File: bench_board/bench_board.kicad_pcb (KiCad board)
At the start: 4 copper layers, 80 x 60 mm, 42 parts, among them J1 BATT_2S, J2 BOOT0_JUMPER, J3 USB-C, J4 CRSF_UART, J5 DSHOT_M1-M4, J6 SWD, U1 STM32F405RGT6, U2 TPS563201, U3 AMS1117-3.3, U4 MPU-6000, U5 USBLC6-2SC6, Y1 8MHz

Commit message: Rework power tree to single-stage buck (3.3V direct); add battery-sense divider
Deletes the AMS1117 5V->3.3V LDO stage and its caps -- the 2-stage
buck-then-LDO topology forced the buck to hold 5V from a 2S pack whose
6.0V floor leaves only 1V of headroom (~83% duty cycle, at/past most buck
ICs' practical limit). TPS563201 now regulates directly to 3.3V (feedback
divider R1/R2 retargeted: 33.2k/10.0k, Vref=0.768V -> ~3.30V), which is
what every load on this board (STM32F405, MPU-6000, DShot signal levels)
actually wants. Duty cycle at 6.0V floor is now ~55%; at 8.4V ceiling
~39% -- comfortable across the whole battery range, both ends far from the
TPS563201's ~90% max-duty limit.

Inductor re-sized for the new operating point: L1 2.2uH -> 10uH, sized for
~23% ripple current at a 1.5A load estimate (worst-case ripple is at
Vin=8.4V, the max input, not the 6.0V floor). C2 (22uF output cap,
unchanged) gives ~7mV ripple at that current, comfortable margin. Thermal
margin is now single-stage only (~0.5W in the buck at 1.5A/90% eff, ~33C
rise in a SOT-23-6 package) instead of also carrying the LDO's dropout
heat, which was the dominant loss term in the old topology.

Also fixed a real latent bug found while touching this circuit: C3, the
TPS563201's SW-to-BOOST bootstrap cap, was 2.2nF -- roughly two orders of
magnitude under the ~100nF a D-CAP2/D-CAP3 synchronous buck needs to hold
the high-side gate charge, especially at the now-much-lower duty cycles.
Corrected to 100nF.

CRSF_UART's receiver-power pin (J4/1) now carries 3V3 instead of the
deleted 5V rail. Per the Build Plan: the many 5V-only ELRS nano receivers
this affects get resolved by picking a 3.3V-capable receiver in Stage 2
part selection, not by adding a rail back.

Battery-sense divider added (genuine prior omission -- no low-voltage
cutoff existed anywhere): R9 (20.0k, VBAT_2S side) / R10 (10.0k, GND
side), 1% resistors, into PA0 (ADC123_IN0, previously unused) with a
100nF filter cap (C22). Divide-by-3.0 r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
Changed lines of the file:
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@@
 		(end 3 0)
 		(stroke
-			(width 0)
+			(width 0.1)
 			(type default)
 		)
@@
 		(end 0 3)
 		(stroke
-			(width 0)
+			(width 0.1)
 			(type default)
 		)
@@
 		(end 77 0)
 		(stroke
-			(width 0)
+			(width 0.1)
 			(type default)
 		)
@@
 		(end 0 57)
 		(stroke
-			(width 0)
+			(width 0.1)
 			(type default)
 		)
@@
 		(end 80 3)
 		(stroke
-			(width 0)
+			(width 0.1)
 			(type default)
 		)
@@
 		(end 3 60)
 		(stroke
-			(width 0)
+			(width 0.1)
 			(type default)
 		)
@@
 		(end 80 57)
 		(stroke
-			(width 0)
+			(width 0.1)
 			(type default)
 		)
@@
 		(end 77 60)
 		(stroke
-			(width 0)
+			(width 0.1)
 			(type default)
 		)

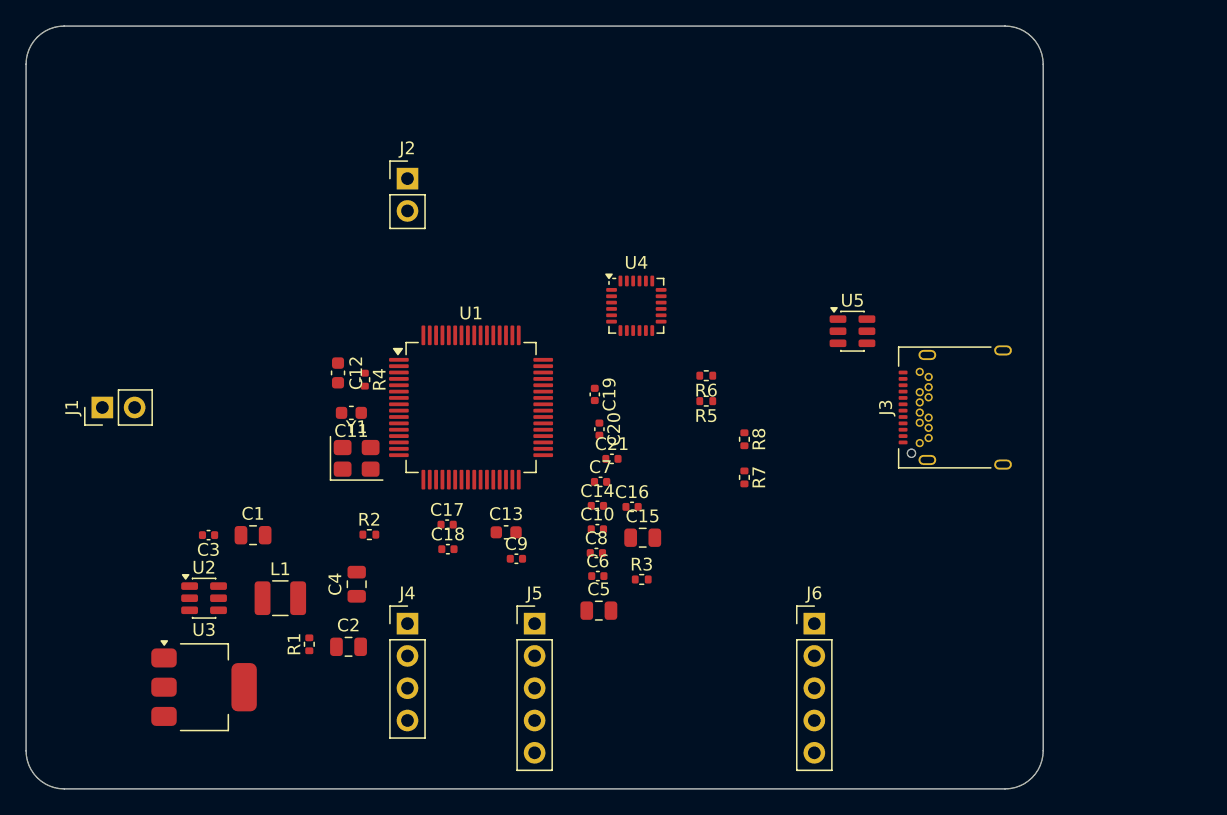
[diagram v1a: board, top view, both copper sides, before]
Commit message: Re-sync PCB from reworked schematic; attempt Freerouting autoroute
PCB was stale since the power-tree rework/battery-sense commit (a16eadb):
sync_schematic_to_board only adds/updates footprints and net assignments,
it does not delete footprints removed from the schematic or refresh Value
text on ones that survived -- confirmed by inspection, not assumed.
Manually closed both gaps: deleted U3/C4/C5 (the removed LDO stage) from
the board, and pushed the schematic's new values onto the PCB (R1
40.2k->33.2k, R2 7.32k->10.0k, L1 2.2uH->10uH, C3 2.2nF->100nF). Placed
the 3 new battery-sense footprints (R9/R10/C22, synced in at the origin,
stacked on top of each other) at (18.5, 26-32.5mm) -- clear of every
existing footprint, just west of the MCU's PA0 pin, verified via
check_courtyard_overlaps before and after the move. 0 courtyard overlaps,
0 boundary violations across all 42 remaining footprints post-edit.

Freerouting (now actually installed -- see wiki/references/tooling-status.md)
attempted end to end: export DSN, route, import SES, run DRC. Two runs,
per Freerouting's own in-log warning that multi-threaded route
optimization is known to generate clearance violations: first multi-
threaded (bench_board.ses), then single-threaded per that recommendation
(bench_board_st.ses, the one actually imported). Both finished identically
at "0 unrouted, 60 violations" per Freerouting's own scoring -- the
threading warning wasn't the actual cause here.

Real result, NOT clean, reported verbatim rather than polished: KiCad DRC
on the imported route (after a zone refill -- the GND pour was stale/
unfilled post-sync) finds 158 violations (130 errors, 28 warnings):
clearance 60, track_width 62, silk_over_copper 17, silk_overlap 11,
copper_edge_clearance 6, hole_clearance 2. Root cause identified, not just
counted: clearance/hole/edge violations (68 of 158) cluster tightly at
the USB-C connector's own fine pad pitch against the board's default
clearance rule -- the same finding as th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
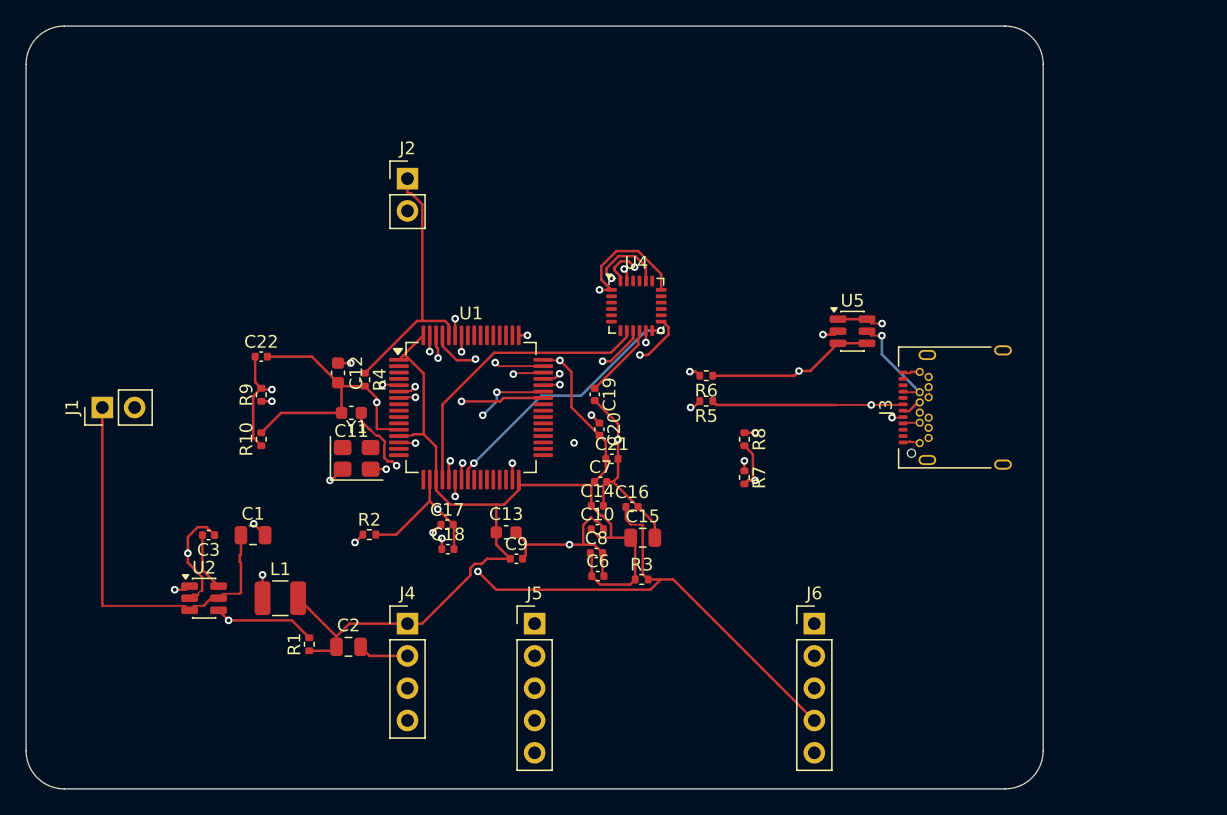
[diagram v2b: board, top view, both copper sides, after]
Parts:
- removed C4: 10uF, Capacitor_SMD:C_0805_2012Metric
- removed C5: 22uF, Capacitor_SMD:C_0805_2012Metric
- removed U3: AMS1117-3.3, Package_TO_SOT_SMD:SOT-223-3_TabPin2
- added C22: 100nF, Capacitor_SMD:C_0402_1005Metric, F.Cu at (18.5, 26.0)
- added R10: 10.0k, Resistor_SMD:R_0402_1005Metric, F.Cu at (18.5, 32.5)
- added R9: 20.0k, Resistor_SMD:R_0402_1005Metric, F.Cu at (18.5, 29.0)
- C3: value 2.2nF -> 100nF
- L1: value 2.2uH -> 10uH
- R1: value 40.2k -> 33.2k
- R2: value 7.32k -> 10.0k
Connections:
- C2 pad 1: 5V -> 3V3
- J4 pad 1: 5V -> 3V3
- L1 pad 2: 5V -> 3V3
- R1 pad 1: 5V -> 3V3
- U1 pad 14: (no net) -> VBAT_SENSE
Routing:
- net 3V3: track 0.00 -> 144.2 mm, vias 0 -> 2
- net GND: track 0.00 -> 92.1 mm, vias 0 -> 11
- net NRST: track 0.00 -> 57.0 mm, vias 0 -> 2
- net SWCLK: track 0.00 -> 48.3 mm, vias 0 -> 1
- net VBAT_2S: track 0.00 -> 47.0 mm, vias 0 -> 1
- net M2: track 0.00 -> 41.5 mm, vias 0 -> 1
- net CRSF_TX: track 0.00 -> 38.6 mm, vias 0 -> 1
- net SWDIO: track 0.00 -> 35.3 mm, vias 0 -> 1
- net M4: track 0.00 -> 33.5 mm, vias 0 -> 1
- net M3: track 0.00 -> 32.7 mm, vias 0 -> 1
- net CRSF_RX: track 0.00 -> 32.6 mm, vias 0 -> 2
- net USB_DM: track 0.00 -> 30.1 mm, vias 0 -> 2
- net SPI1_MOSI: track 0.00 -> 26.9 mm, vias 0 -> 2
- net USB_DP: track 0.00 -> 25.3 mm, vias 0 -> 1
- net M1: track 0.00 -> 25.1 mm, vias 0 -> 1
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
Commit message: Checkpoint: autoroute run + DRC that exposed a stale board (documented dirty)
Autoroute completed (621 tracks, 86 vias, all 6 target nets, 4 attempts
all converging on score 69501). Then DRC, run with --schematic-parity,
came back 267 violations / 10 unconnected / 264 parity issues -- and the
parity report explains the whole thing.

THE BOARD WAS NEVER RE-SYNCED FROM THE SCHEMATIC. The PCB still carries
the 2S-era power section:

  ref | board (stale)                | schematic (current)
  ----+------------------------------+---------------------------
  U2  | TPS563201, SOT-23-6, 6 pads  | TPS54336ADDA, SOIC-8-1EP
  J1  | BATT_2S                      | BATT_4S
  R1  | 33.2k                        | 31.6k
  R9  | 20.0k                        | 75.0k

R1/R9 are the feedback divider that sets the output voltage, so this is
not cosmetic drift -- the board encodes a different regulator at a
different output voltage than the schematic specifies.

It also explains the rest of the report. All 5 shorting_items land on a
U2 pad, because the router was connecting a SOIC-8 netlist to SOT-23-6
pad numbers -- pad 2/4/6 mean different things on the two packages. The
199 net_conflicts are the '/'-prefixed sheet-path form. The 65
track_width violations are 0.15mm legacy USB traces against a 0.2mm
minimum. The 4 missing_footprint entries are PWR_FLAGs and are benign.

Committing the dirty state deliberately, per the batch rule that a
documented-dirty DRC beats a faked-clean one. The routing produced above
is INVALID and is superseded by the re-sync in the next commit.

This is the same duplication-drift failure this project keeps hitting --
params.c, the mixer defaults, the ground-station decoder -- showing up
in hardware for the first time: two artifacts describing one thing, only
one of them updated.

Co-Authored-By: Claude Opus 5 <noreply@anthropic.com>
Claude-Session: https://claude.ai/code/session_013j3hUNiKQb8Wi66Tf5nVkP
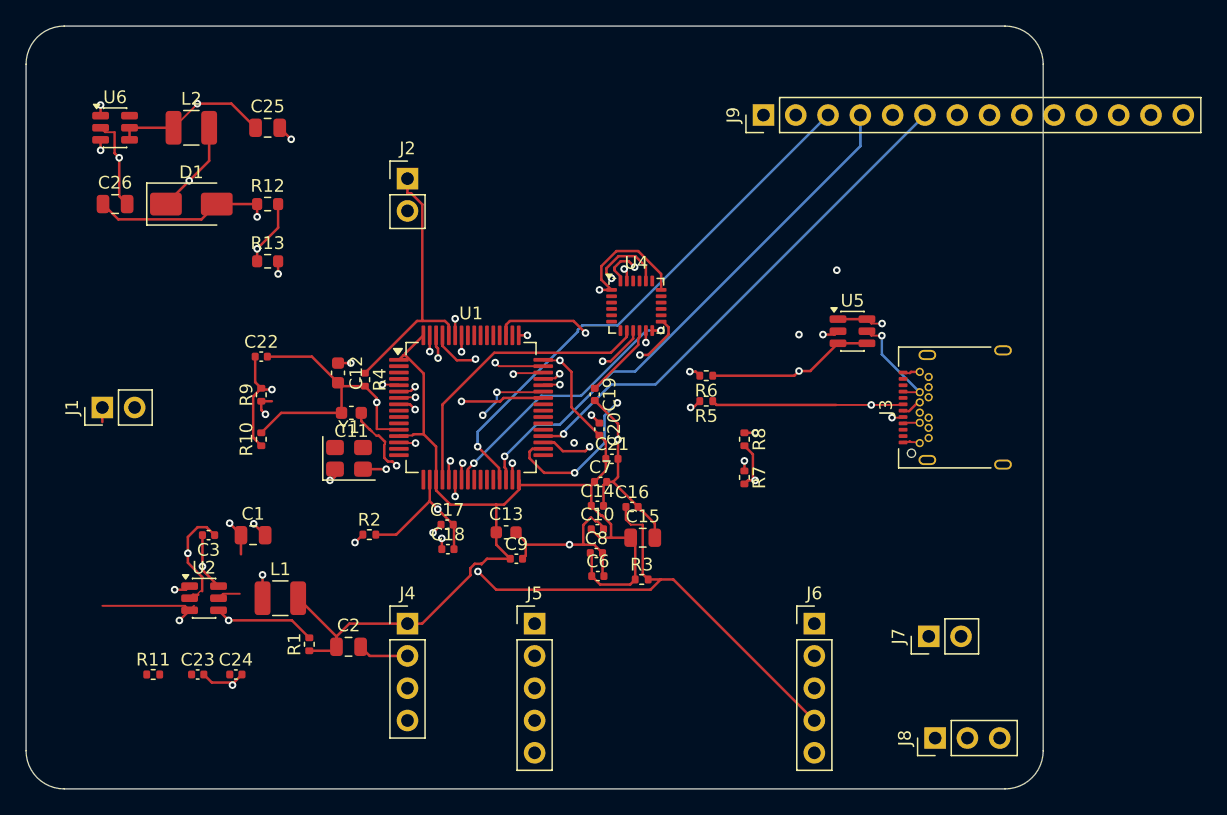
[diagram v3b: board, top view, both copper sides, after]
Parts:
- added C23: 7.5nF, Capacitor_SMD:C_0402_1005Metric, F.Cu at (13.5, 51.0)
- added C24: 10nF, Capacitor_SMD:C_0402_1005Metric, F.Cu at (16.5, 51.0)
- added C25: 10uF 16V, Capacitor_SMD:C_0805_2012Metric, F.Cu at (19.0, 8.00)
- added C26: 22uF 16V, Capacitor_SMD:C_0805_2012Metric, F.Cu at (7.00, 14.0)
- added D1: SS34, Diode_SMD:D_SMA, F.Cu at (13.0, 14.0)
- added J7: RX_PWR_5V, Connector_PinHeader_2.54mm:PinHeader_1x02_P2.54mm_Vertical, F.Cu at (71.0, 48.0)
- added J8: TELEM_TX, Connector_PinHeader_2.54mm:PinHeader_1x03_P2.54mm_Vertical, F.Cu at (71.5, 56.0)
- added J9: EXPANSION_BUS, Connector_PinHeader_2.54mm:PinHeader_1x14_P2.54mm_Vertical, F.Cu at (58.0, 7.00)
- added L2: 10uH, Inductor_SMD:L_1210_3225Metric, F.Cu at (13.0, 8.00)
- added R11: 2k, Resistor_SMD:R_0402_1005Metric, F.Cu at (10.0, 51.0)
- added R12: 73.2k, Resistor_SMD:R_0603_1608Metric, F.Cu at (19.0, 14.0)
- added R13: 10.0k, Resistor_SMD:R_0603_1608Metric, F.Cu at (19.0, 18.5)
- added U6: MT3608, Package_TO_SOT_SMD:SOT-23-6, F.Cu at (7.00, 8.00)
- moved Y1 0.60 mm to (25.4, 34.0)
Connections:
- C1 pad 1: VBAT_2S -> VBAT_4S
- J1 pad 1: VBAT_2S -> VBAT_4S
- R9 pad 1: VBAT_2S -> VBAT_4S
- U1 pad 10: (no net) -> EXP_IRQ1
- U1 pad 11: (no net) -> EXP_IRQ2
- U1 pad 29: (no net) -> EXP_I2C_SCL
- U1 pad 30: (no net) -> EXP_I2C_SDA
- U1 pad 34: (no net) -> EXP_SPI_SCK
- U1 pad 35: (no net) -> EXP_SPI_MISO
- U1 pad 36: (no net) -> EXP_SPI_MOSI
- U1 pad 51: (no net) -> TELEM_TX
- U1 pad 52: (no net) -> EXP_UART_RX
- U1 pad 8: (no net) -> EXP_SPI_CS1
- U1 pad 9: (no net) -> EXP_SPI_CS2
- U2 pad 1: GND -> VBST_NODE
- U2 pad 2: SW_NODE -> VBAT_4S
- U2 pad 3: VBAT_2S -> SW_NODE
- U2 pad 4: VFB -> GND
- U2 pad 5: VBAT_2S -> VFB
- U2 pad 6: VBST_NODE -> COMP_NODE
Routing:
- net 5V_RX: track 0.00 -> 93.3 mm, vias 0 -> 2
- net 3V3: track 144.2 -> 226.1 mm, vias 2 -> 3
- net EXP_SPI_CS1: track 0.00 -> 70.4 mm, vias 0 -> 1
- net TELEM_TX: track 0.00 -> 60.9 mm, vias 0 -> 2
- net VBAT_2S: track 47.0 -> 0.00 mm, vias 1 -> 0
- net EXP_SPI_MISO: track 0.00 -> 46.5 mm, vias 0 -> 1
- net EXP_SPI_SCK: track 0.00 -> 46.0 mm, vias 0 -> 2
- net EXP_I2C_SCL: track 0.00 -> 42.4 mm, vias 0 -> 1
- net EXP_I2C_SDA: track 0.00 -> 42.4 mm, vias 0 -> 1
- net EXP_SPI_MOSI: track 0.00 -> 40.6 mm, vias 0 -> 1
- net VBAT_4S: track 0.00 -> 31.1 mm, vias 0 -> 2
- net VFB_5V: track 0.00 -> 21.5 mm, vias 0 -> 2
- net BOOST_SW: track 0.00 -> 17.7 mm, vias 0 -> 2
- net SW_NODE: track 17.1 -> 31.3 mm, vias 2 -> 3
- net GND: track 92.1 -> 104.1 mm, vias 11 -> 14
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
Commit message: Re-sync board to schematic, replace U2 properly, add In2 plane, re-route
Fixes the stale-board defect from the previous commit. Full write-up in
docs/stale-board-resync-2026-08-17.md.

What changed:
  - U2 DELETED and re-placed from the library. Renaming the footprint
    field via edit_component was not enough and was actively harmful:
    it left the SOT-23-6's six lands under a SOIC-8 name, so the board
    was equally wrong but no longer advertised it. Correct geometry is
    13 pads (8 signal + thermal EP + 4 EP stitching).
  - J1/R1/R9/C1 values corrected to match the schematic. A scripted
    board-vs-schematic diff now shows zero value and zero footprint
    drift across all 55 parts.
  - J9 was hanging 12.8mm off the right board edge; moved to x=43,
    validated with check_courtyard_overlaps first (0 overlaps).
  - In2.Cu had no pour. Added a 3V3 plane; Freerouting then detected
    BOTH inner layers as dedicated power planes.
  - Added a Power netclass (0.6mm track, 0.8/0.4 via) for VBAT_4S,
    3V3, 5V_RX, GND, SW_NODE, BOOST_SW; everything had been at 0.2mm.
  - Design rules aligned to JLCPCB 4-layer capability (0.127mm
    clearance, 0.15mm min track, 0.3mm edge) because the previous
    0.25mm rule was stricter than the parts' own geometry -- a
    0.5mm-pitch LQFP has 0.2mm pad gaps by construction.

Routing improved across the three runs: 19 nets -> 45 -> ALL 51.
498 tracks, 89 vias.

DRC, verbatim and NOT clean:

  Found 43 violations
  Found 19 unconnected items
  Found 258 schematic parity issues

  silk_over_copper 17, silk_overlap 13, clearance 8,
  starved_thermal 3, copper_edge_clearance 2

Down from 267/10/264 at the start of this work. shorting_items went
5 -> 0, footprint_symbol_mismatch 6 -> 0, lib_footprint_mismatch 1 -> 0.
Every remaining copper violation is on J3 (USB-C): internal pad-to-pad
spacing inside the manufacturer's footprint, and its mounting pads near
the edge.

THE 19 UNCONNECTED ARE REAL AND BLOCK FABRICATION. They are mos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
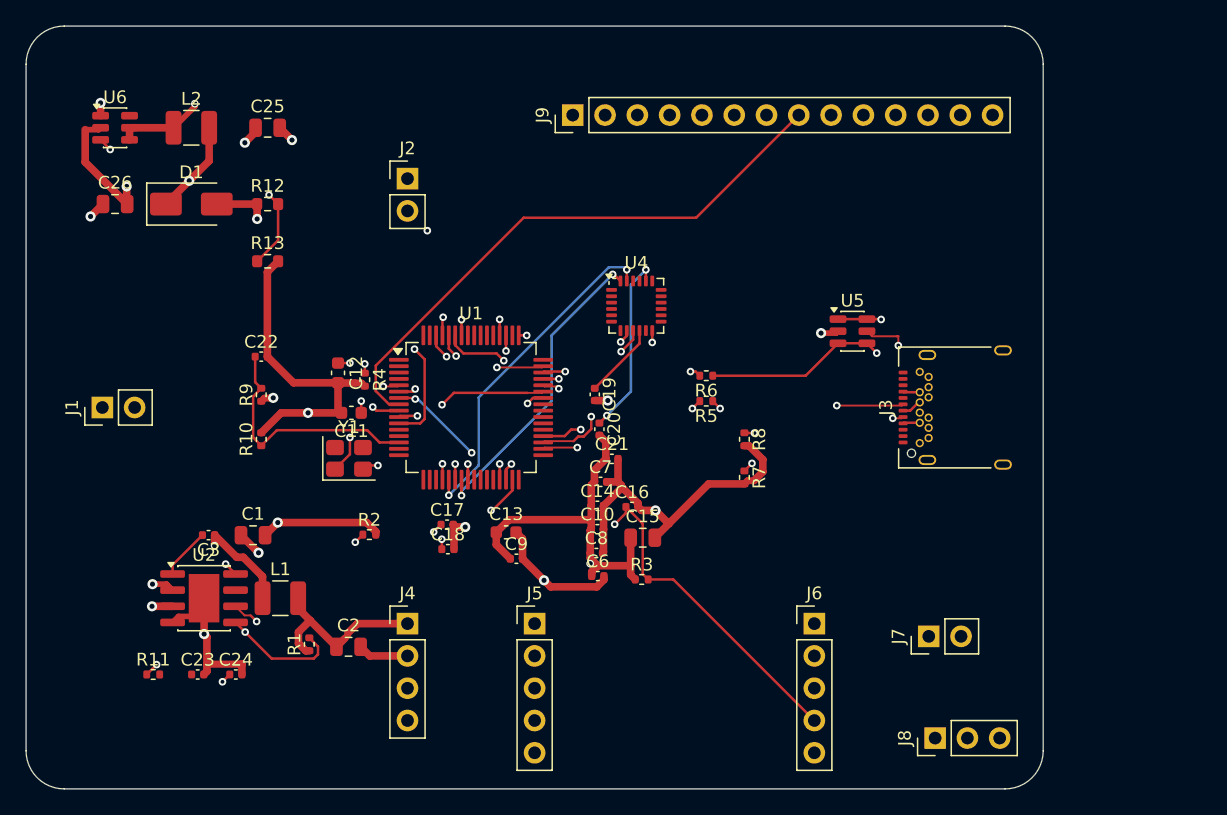
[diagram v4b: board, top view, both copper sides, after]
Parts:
- C1: value 10uF -> 10uF 35V
- J1: value BATT_2S -> BATT_4S
- R1: value 33.2k -> 31.6k
- R9: value 20.0k -> 75.0k
- U2: value TPS563201 -> TPS54336ADDA; footprint Package_TO_SOT_SMD:SOT-23-6 -> Package_SO:SOIC-8-1EP_3.9x4.9mm_P1.27mm_EP2.41x3.81mm
- moved J9 15.0 mm to (43.0, 7.00)
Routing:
- net 3V3: track 226.1 -> 52.3 mm
- net EXP_IRQ2: track 0.00 -> 56.0 mm, vias 0 -> 1
- net EXP_IRQ1: track 0.00 -> 54.5 mm, vias 0 -> 1
- net EXP_SPI_CS2: track 0.00 -> 53.3 mm, vias 0 -> 2
- net EXP_UART_RX: track 0.00 -> 36.5 mm, vias 0 -> 1
- net 5V_RX: track 93.3 -> 120.8 mm
- net EXP_SPI_CS1: track 70.4 -> 45.7 mm, vias 1 -> 0
- net SW_NODE: track 31.3 -> 16.2 mm, vias 3 -> 2
- net COMP_NODE: track 0.00 -> 12.9 mm, vias 0 -> 2
- net EXP_SPI_MISO: track 46.5 -> 34.6 mm
- net EXP_SPI_SCK: track 46.0 -> 34.6 mm, vias 2 -> 1
- net VBAT_4S: track 31.1 -> 42.3 mm, vias 2 -> 3
- net SS_NODE: track 0.00 -> 11.3 mm, vias 0 -> 2
- net TELEM_TX: track 60.9 -> 49.9 mm, vias 2 -> 1
- net M2: track 41.5 -> 30.6 mm
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- added copper zone on In2.Cu, net 3V3
